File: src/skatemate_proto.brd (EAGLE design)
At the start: 160 x 100 mm, 58 parts, among them IC1 REG1117, Q1 IRF740, Q2 IRF740, Q3 IRF740, Q4 IRF740, Q5 IRF740, Q6 IRF740, U1 DRV8301DCAR

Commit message: Further routing
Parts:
- added TP1, TP2, TP3, TP4, TP5: TPSMD_M_1006, skatemate:SMD_M_1006
- moved R12 116.7 mm to (50.5, 20.8)
- moved D3 110.5 mm to (55.6, 23.4), turned to 180 degrees
- moved R9 107.6 mm to (55.6, 46.2)
- moved R10 106.5 mm to (50.5, 46.2)
- moved C13 103.9 mm to (40.4, 42.4), turned to 90 degrees
- moved R11 100.5 mm to (55.6, 20.8)
- moved C2 100.1 mm to (35.8, 36.6), turned to 270 degrees
- moved C12 98.8 mm to (40.4, 46.5), turned to 90 degrees
- moved D2 98.0 mm to (55.6, 48.8), turned to 180 degrees
- moved C1 97.7 mm to (38.4, 36.6), turned to 90 degrees
- moved R7 96.7 mm to (55.6, 71.6)
- moved R8 96.7 mm to (50.5, 71.6)
- moved C11 93.9 mm to (40.4, 50.5), turned to 90 degrees
- moved D1 91.4 mm to (55.6, 74.2), turned to 180 degrees
- moved C5 87.7 mm to (50.5, 23.4), turned to 180 degrees
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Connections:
- net GND: now also TP2.P$1
- net PH_A: now also TP3.P$1
- net PH_B: now also TP4.P$1
- net PH_C: now also TP5.P$1
- net SUPPLY: now also TP1.P$1
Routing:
- net PH_A: track 0.00 -> 46.5 mm
- net PH_C: track 0.00 -> 46.2 mm
- net PH_B: track 0.00 -> 45.9 mm
- net SUPPLY: track 0.00 -> 26.7 mm
- net GND: track 0.00 -> 18.3 mm, vias 0 -> 3
- net GH_A: track 0.00 -> 9.72 mm
- net GL_C: track 0.00 -> 9.42 mm
- net GH_B: track 0.00 -> 9.34 mm
- net GL_A: track 0.00 -> 9.30 mm
- net GH_C: track 0.00 -> 8.89 mm
- net N$13: track 0.00 -> 8.70 mm
- net GL_B: track 0.00 -> 8.67 mm
- net ASENSE: track 0.00 -> 8.15 mm
- net CSENSE: track 0.00 -> 8.15 mm
- net BSENSE: track 0.00 -> 8.15 mm
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- added copper zone on layer 16, net GND
- added copper zone on layer 16, net SUPPLY

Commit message: Test
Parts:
- moved C24 72.9 mm to (18.0, 10.7)
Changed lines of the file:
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@@
 <?xml version="1.0" encoding="utf-8"?>
 <!DOCTYPE eagle SYSTEM "eagle.dtd">
-<eagle version="7.6.0">
+<eagle version="7.5.0">
 <drawing>
 <settings>
@@
 <element name="C22" library="skatemate" package="B/3528-21W" value="100u" x="23.622" y="65.278"/>
 <element name="C23" library="skatemate" package="B/3528-21W" value="100u" x="7.112" y="63.754" rot="R90"/>
-<element name="C24" library="skatemate" package="C0805" value="0.1u" x="-41.91" y="52.07"/>
+<element name="C24" library="skatemate" package="C0805" value="0.1u" x="18.034" y="10.668"/>
 <element name="C3" library="skatemate" package="C0805" value="" x="50.546" y="74.168" rot="R180"/>
 <element name="C4" library="skatemate" package="C0805" value="" x="50.546" y="48.768" rot="R180"/>
@@
 <wire x1="-17.46" y1="45.72" x2="7.112" y2="62.129" width="0" layer="19" extent="1-1"/>
 <wire x1="-23.81" y1="45.72" x2="-17.46" y2="45.72" width="0" layer="19" extent="1-1"/>
-<wire x1="-40.96" y1="52.07" x2="-23.81" y2="45.72" width="0" layer="19" extent="1-1"/>
-<wire x1="-59.69" y1="-15.24" x2="-40.96" y2="52.07" width="0" layer="19" extent="1-1"/>
+<wire x1="18.984" y1="10.668" x2="-23.81" y2="45.72" width="0" layer="19" extent="1-1"/>
+<wire x1="-59.69" y1="-15.24" x2="18.984" y2="10.668" width="0" layer="19" extent="1-1"/>
 </signal>
 <signal name="N$7">
@@
 <wire x1="-40.96" y1="45.72" x2="-34.61" y2="45.72" width="0" layer="19" extent="1-1"/>
 <wire x1="-47.31" y1="45.72" x2="-40.96" y2="45.72" width="0" layer="19" extent="1-1"/>
-<wire x1="-42.86" y1="52.07" x2="-40.96" y2="45.72" width="0" layer="19" extent="1-1"/>
+<wire x1="17.084" y1="10.668" x2="-40.96" y2="45.72" width="0" layer="19" extent="1-1"/>
 </signal>
 <signal name="INH_A">

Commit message: links es bezzeli
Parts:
- moved TP2 91.5 mm to (8.38, 46.0)
- moved TP1 80.9 mm to (8.38, 37.3)
- moved R19 68.4 mm to (19.6, 54.6), turned to 180 degrees
- moved R18 58.2 mm to (16.0, 51.8), turned to 270 degrees
- moved R17 55.5 mm to (19.6, 52.1), turned to 180 degrees
- moved R15 44.0 mm to (13.5, 56.4), turned to 90 degrees
- moved C24 42.0 mm to (9.65, 51.8), turned to 180 degrees
- moved R14 40.3 mm to (16.0, 56.4), turned to 270 degrees
- moved R16 37.8 mm to (19.6, 57.1)
- moved C21 8.64 mm to (38.4, 35.6)
- moved C20 8.38 mm to (35.8, 35.6)
- moved C1 5.18 mm to (43.4, 35.6), turned to 270 degrees
- moved C2 5.18 mm to (40.9, 35.6)
- moved C17 5.00 mm to (17.0, 38.9), turned to 0 degrees
- moved C9 4.91 mm to (17.0, 43.9), turned to 0 degrees
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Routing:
- net GND: track 18.3 -> 82.4 mm
- net VCC: track 0.00 -> 46.4 mm
- net SUPPLY: track 26.7 -> 61.7 mm
- net +5V: track 0.00 -> 30.2 mm
- net N$4: track 0.00 -> 16.1 mm
- net DRV_NOCTW: track 0.00 -> 12.0 mm
- net N$2: track 0.00 -> 10.8 mm
- net N$6: track 0.00 -> 9.28 mm
- net N$1: track 0.00 -> 8.50 mm
- net DRV_PWRGD: track 0.00 -> 8.06 mm
- net N$17: track 0.00 -> 7.50 mm
- net N$18: track 0.00 -> 7.49 mm
- net BST_BK: track 0.00 -> 6.60 mm
- net DRV_NFAULT: track 0.00 -> 6.09 mm
- net N$3: track 0.00 -> 4.94 mm

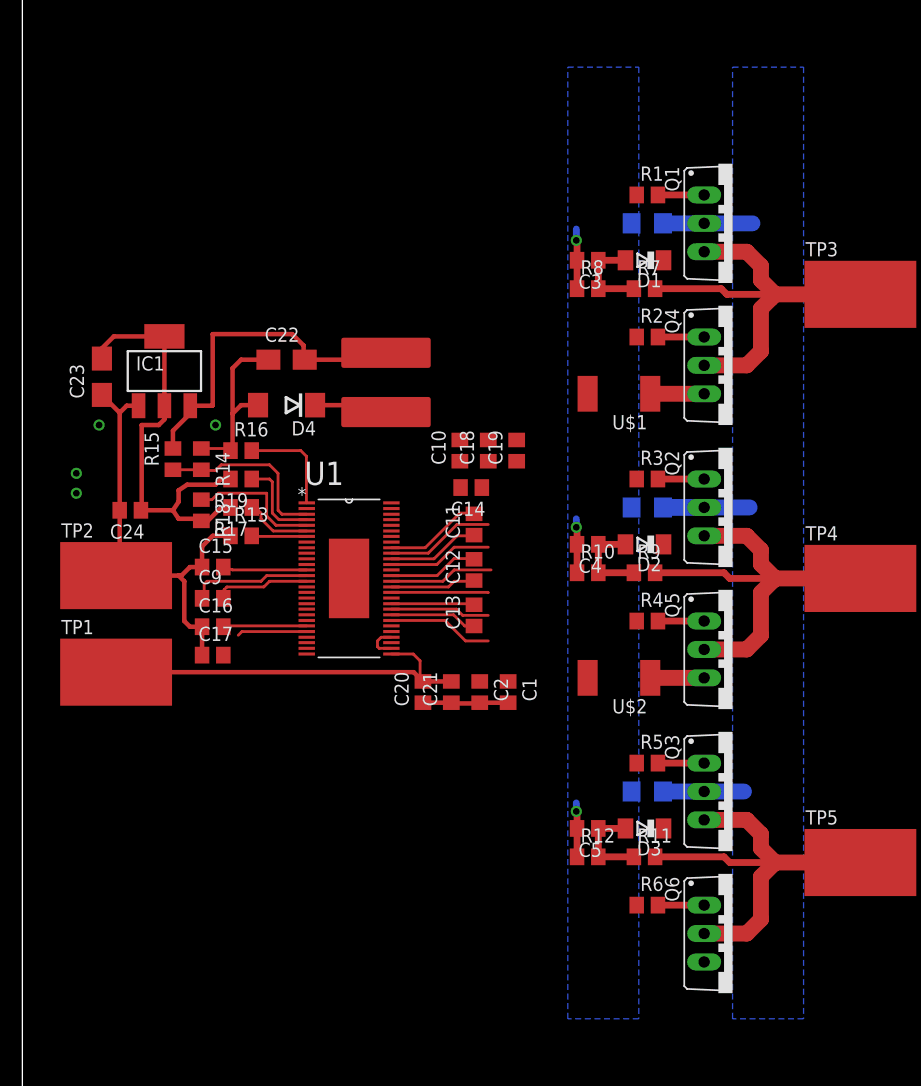
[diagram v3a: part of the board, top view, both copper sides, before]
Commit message: Leistungsstufe weiter geroutet
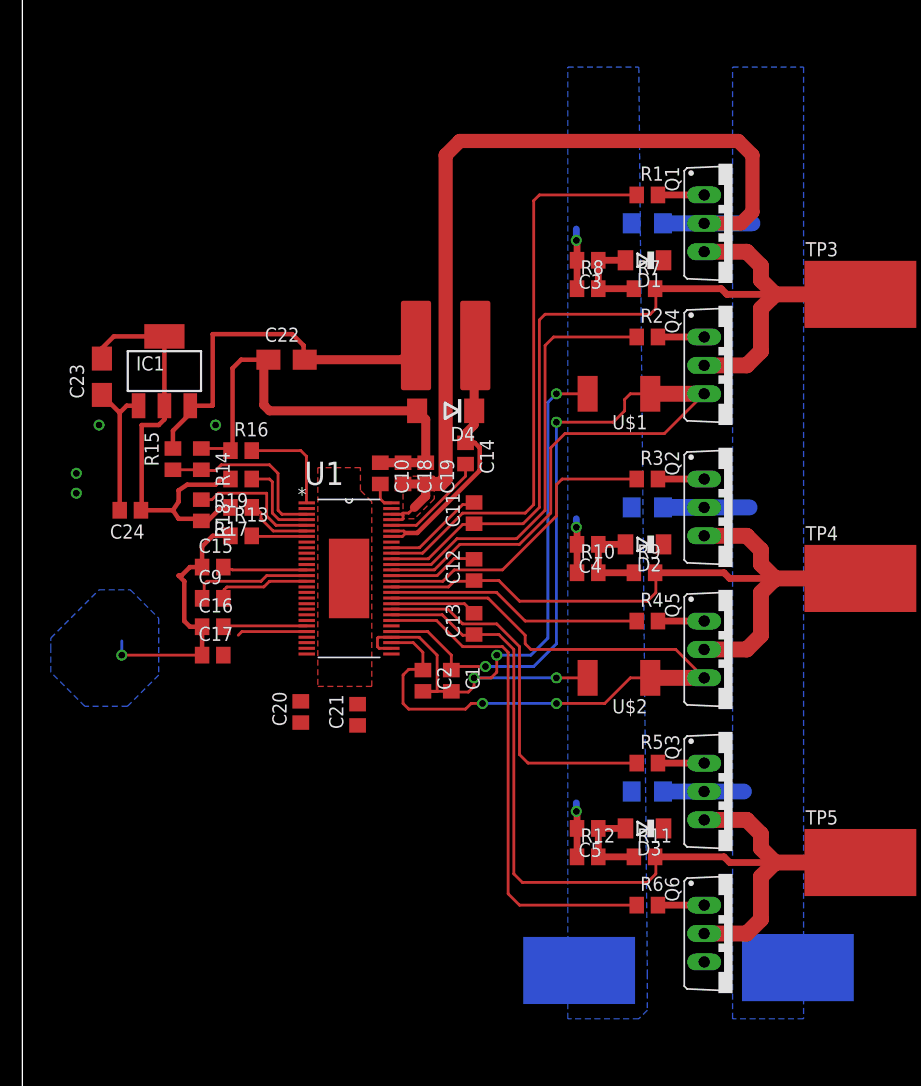
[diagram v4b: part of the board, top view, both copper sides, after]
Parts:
- moved TP1 66.4 mm to (69.3, 10.9), flipped to the bottom
- moved TP2 54.4 mm to (49.8, 10.7), flipped to the bottom
- moved D4 14.2 mm to (37.8, 60.7)
- moved C20 11.1 mm to (24.9, 33.8)
- moved C21 8.62 mm to (30.0, 33.5)
- moved C19 8.38 mm to (36.1, 55.1), turned to 270 degrees
- moved C18 7.89 mm to (34.0, 55.1), turned to 270 degrees
- moved C10 7.40 mm to (32.0, 55.1), turned to 270 degrees
- moved L1 6.27 mm to (37.8, 66.5), turned to 270 degrees
- moved C1 5.18 mm to (38.4, 36.6)
- moved C2 5.18 mm to (35.8, 36.6)
- moved C14 3.09 mm to (39.6, 56.9), turned to 270 degrees
- moved C11 1.02 mm to (40.4, 51.6)
- moved C13 0.76 mm to (40.4, 41.7)
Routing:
- net SN_A: track 4.82 -> 90.5 mm, vias 0 -> 2
- net GND: track 82.4 -> 155.1 mm, vias 3 -> 8
- net SN_B: track 4.82 -> 69.0 mm, vias 0 -> 2
- net SUPPLY: track 61.7 -> 104.2 mm
- net GH_A: track 9.72 -> 51.1 mm
- net PH_C: track 46.2 -> 85.6 mm
- net PH_A: track 46.5 -> 82.8 mm
- net GL_C: track 9.42 -> 45.1 mm
- net GL_A: track 9.30 -> 39.0 mm
- net GH_C: track 8.89 -> 33.3 mm
- net PH_B: track 45.9 -> 65.1 mm
- net GH_B: track 9.34 -> 27.8 mm
- net BST_BK: track 6.60 -> 24.3 mm
- net GL_B: track 8.67 -> 23.0 mm
- net N$16: track 0.00 -> 9.53 mm
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- added copper zone on layer 1, net GND
- added copper zone on layer 1, net SUPPLY

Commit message: Large junk of routing logic
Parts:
- added C25: (no value), skatemate:C0805
- added C26: 6n8, skatemate:C0805
- added C27: 120p, skatemate:C0805
- added D5: (no value), skatemate:SOD80C
- added R20, R21: (no value), skatemate:R0805
- added R22: 15k, skatemate:R0805
- added SV1, SV2: (no value), skatemate:MA12-1
- moved D1 66.0 mm to (29.2, 13.7), turned to 0 degrees
- moved D2 46.8 mm to (29.2, 10.2), turned to 0 degrees
- moved D3 31.3 mm to (29.2, 6.60), turned to 0 degrees
- moved R15 17.3 mm to (28.2, 65.5)
- moved R17 13.7 mm to (6.86, 47.0), turned to 0 degrees
- moved R14 13.2 mm to (28.2, 61.5), turned to 90 degrees
- moved R19 13.0 mm to (6.86, 52.1), turned to 0 degrees
- moved C24 12.3 mm to (6.86, 63.8), turned to 270 degrees
- moved C17 11.4 mm to (28.2, 36.8)
- moved R18 9.43 mm to (6.86, 49.5), turned to 0 degrees
- moved C22 8.84 mm to (32.0, 62.5), turned to 90 degrees
- moved R16 6.19 mm to (25.4, 55.1), turned to 270 degrees
- moved C9 5.80 mm to (14.2, 38.9), turned to 90 degrees
- moved C16 5.04 mm to (20.8, 38.1)
- moved IC1 3.10 mm to (15.2, 66.0)
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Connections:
- new net N$20: C27.1, R22.2, U1.2
- new net N$21: C26.1, R22.1
- new net SSENSE: C25.1, D5.A, R20.1, R21.2, SV2.12
- net +5V: now also SV1.2
- net ASENSE: now also SV2.9
- net BSENSE: now also SV2.10
- net CSENSE: now also SV2.11
- net DRV_DCCAL: now also SV1.11
- net DRV_EN_GATE: now also SV1.12
- net DRV_NCS: now also SV1.7
- net DRV_NFAULT: now also SV1.6
- net DRV_NOCTW: now also SV1.5
- net DRV_PWRGD: now also SV1.4
- net DRV_SCK: now also SV1.10
- net DRV_SDI: now also SV1.8
- net DRV_SDO: now also SV1.9
- net DRV_SOA: now also SV2.7
- net DRV_SOB: now also SV2.8
- net GND: now also C25.2, C26.2, C27.2, R21.1, SV1.3
- net INH_A: now also SV2.1
- net INH_B: now also SV2.3
- net INH_C: now also SV2.5
- net INL_A: now also SV2.2
- net INL_B: now also SV2.4
- net INL_C: now also SV2.6
- net SUPPLY: now also R20.2
- net VCC: now also D5.C, SV1.1
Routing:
- net ASENSE: track 8.15 -> 109.6 mm, vias 0 -> 2
- net BSENSE: track 8.15 -> 88.1 mm, vias 0 -> 2
- net CSENSE: track 8.15 -> 71.9 mm, vias 0 -> 2
- net SSENSE: track 0.00 -> 51.0 mm
- net GND: track 155.1 -> 106.0 mm, vias 8 -> 24
- net DRV_SOB: track 0.00 -> 48.5 mm
- net DRV_SOA: track 0.00 -> 46.6 mm
- net VCC: track 46.4 -> 3.06 mm, vias 0 -> 1
- net INL_C: track 0.00 -> 43.4 mm
- net INH_C: track 0.00 -> 41.5 mm
- net INL_B: track 0.00 -> 39.4 mm
- net INH_B: track 0.00 -> 37.6 mm
- net INL_A: track 0.00 -> 35.5 mm
- net INH_A: track 0.00 -> 33.5 mm
- net DRV_DCCAL: track 0.00 -> 32.5 mm
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- added copper zone on layer 1, net +5V
- added copper zone on layer 1, net VCC

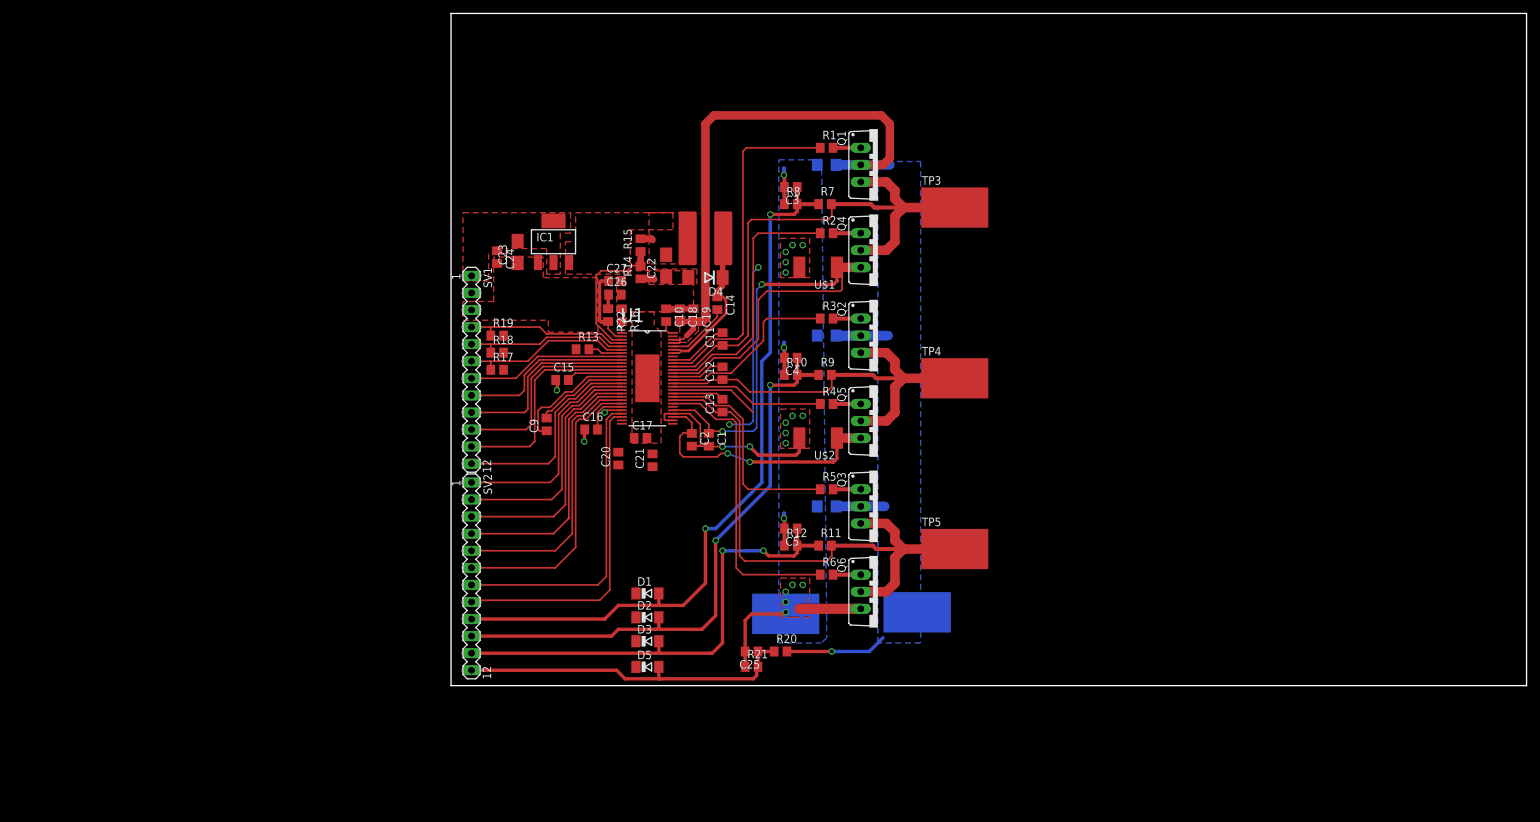
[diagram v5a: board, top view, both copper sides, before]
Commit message: Added uC
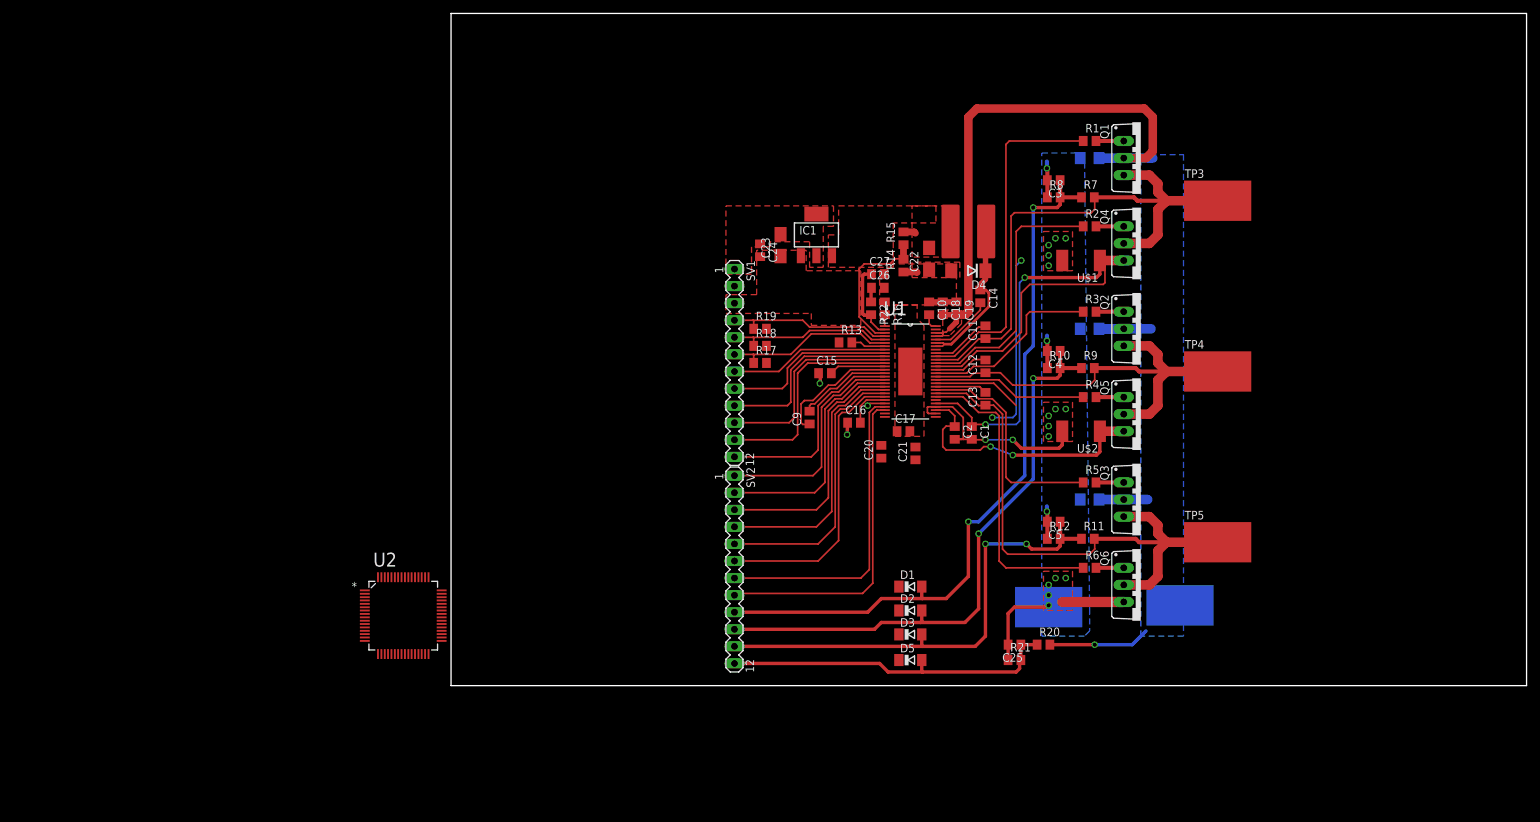
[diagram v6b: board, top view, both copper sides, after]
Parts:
- added U2: STM32F303RCT6, skatemate:QFP50P1200X1200X160-64N
- moved C10 39.1 mm to (71.1, 56.1)
- moved C2 39.1 mm to (74.9, 37.6)
- moved C22 39.1 mm to (71.1, 63.5)
- moved C3 39.1 mm to (89.7, 75.2)
- moved C4 39.1 mm to (89.7, 49.8)
- moved C5 39.1 mm to (89.7, 24.4)
- moved D4 39.1 mm to (77.0, 61.7)
- moved L1 39.1 mm to (77.0, 67.6)
- moved R10 39.1 mm to (89.7, 47.2)
- moved R11 39.1 mm to (94.7, 21.8)
- moved R12 39.1 mm to (89.7, 21.8)
- moved R16 39.1 mm to (64.5, 56.1)
- moved R20 39.1 mm to (88.1, 6.10)
- moved R7 39.1 mm to (94.7, 72.6)
- moved R8 39.1 mm to (89.7, 72.6)
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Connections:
- new net VBAT: U2.1
- new net VDDA: U2.13
- new net VDD_1: U2.64
- new net VDD_2: U2.32
- new net VDD_3: U2.48
- new net VDD_4: U2.19
- new net VSSA/VREF-: U2.12
